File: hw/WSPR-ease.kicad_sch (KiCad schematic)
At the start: 53 parts, among them J101 SMA, J102 SMA, J1301 pwr+data, Q101 MMBF170, U101 GNSS module, U102 ESP32-S3-WROOM-1-N8R8, U103 TPS22918DBVR, U104 TPS74612PQWDRBRQ1, U105 SRV05-4, U106 LMR51430YDDCR

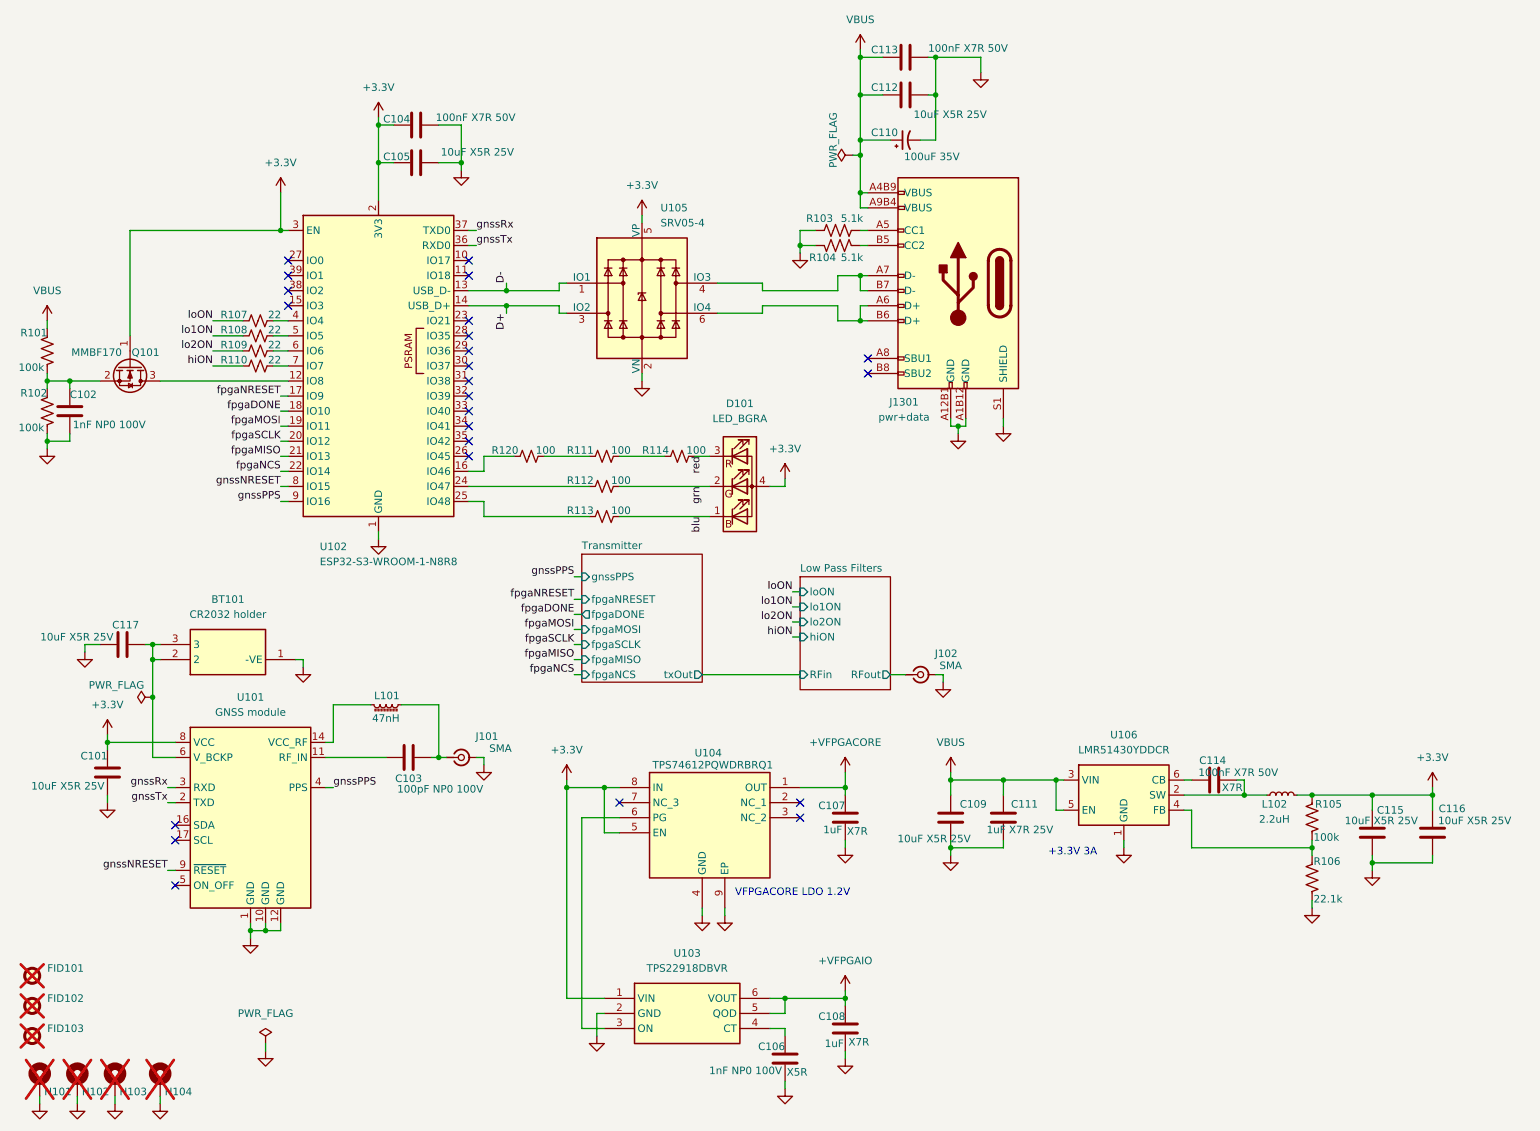
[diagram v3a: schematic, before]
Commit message: Fix huge oopsie with USB diode protection after having fixed the unforgivable polarity reversal and NOT SEEING THIS BUG. I can be an idiot sometimes.
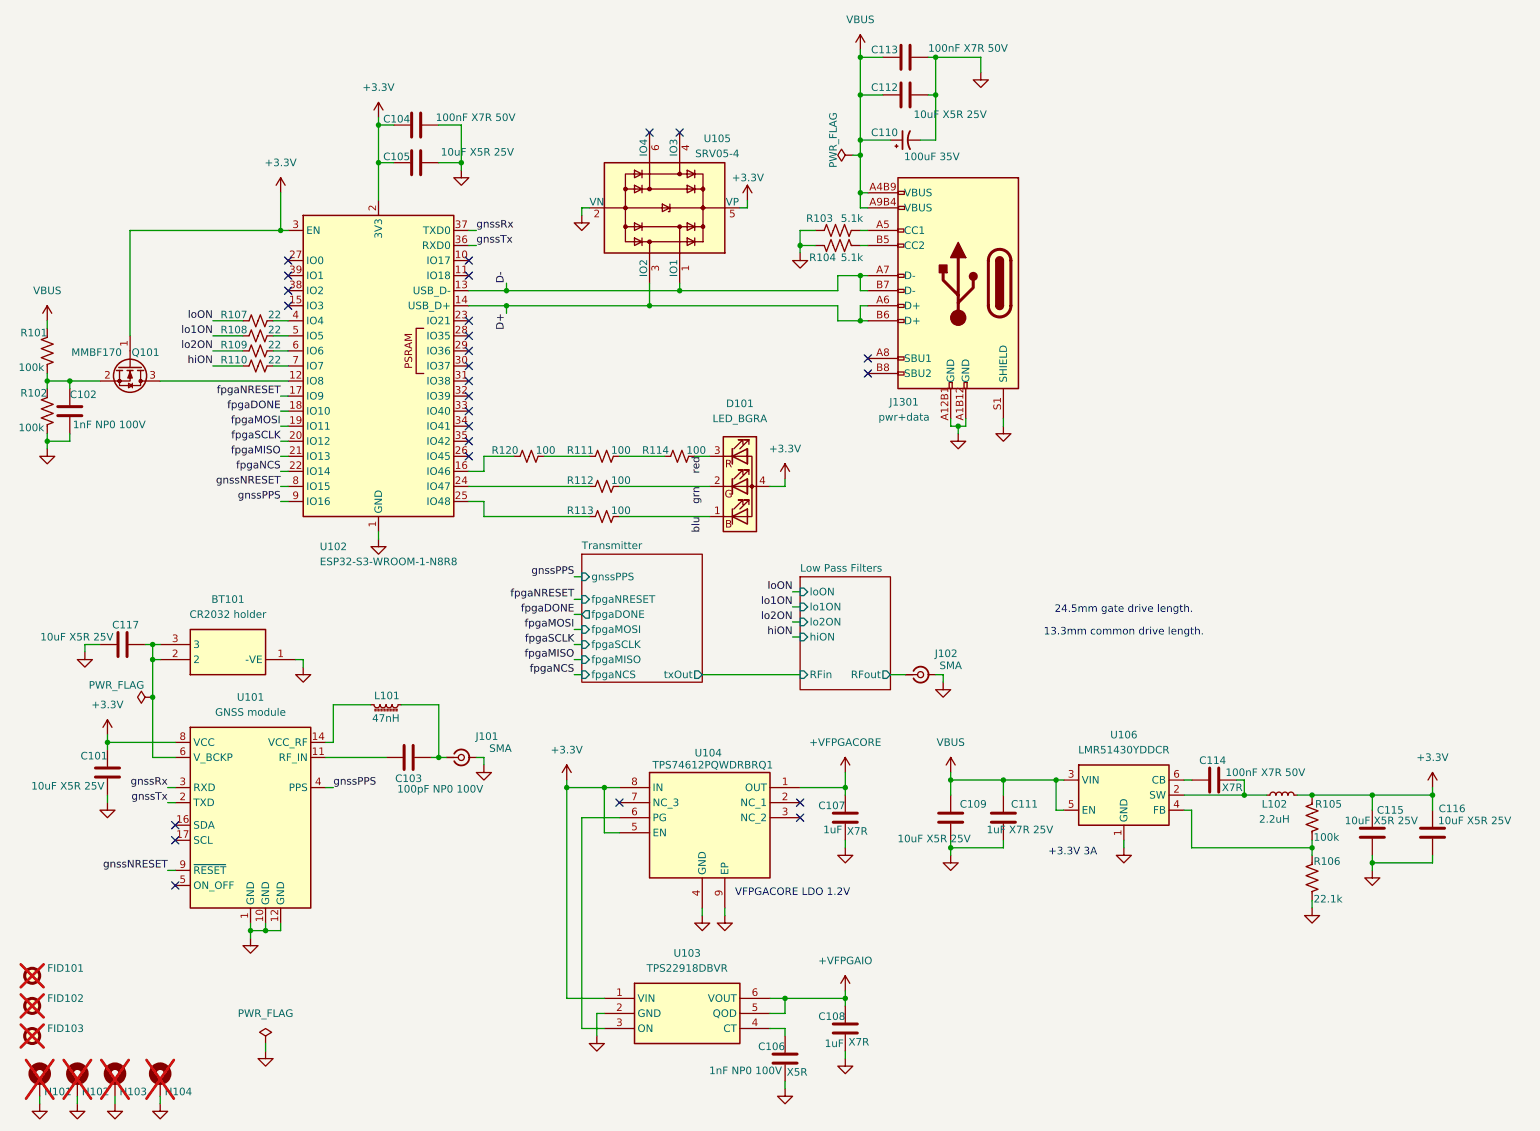
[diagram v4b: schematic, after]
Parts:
- D101: MFG (none) -> Cree; MPN (none) -> UHD111A-FKA-C3K23E1L3VG5ZB3Z3; Mouser_PN (none) -> 941-UHD1AA3K3E3V53Z3
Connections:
- net D+: now also J1301.A6 (D+), J1301.B6 (D+)
- net D-: now also J1301.A7 (D-), J1301.B7 (D-)
- now unconnected: U105.4 (IO3), U105.6 (IO4)
- no-connect marks 24 -> 26
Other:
- note added: "13.3mm common drive length."
- note added: "24.5mm gate drive length."
- moved on the sheet: U105
